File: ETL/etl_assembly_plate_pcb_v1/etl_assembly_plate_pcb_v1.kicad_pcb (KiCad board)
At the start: 2 copper layers, 203.2 x 114.3 mm, 86 parts, among them IC1 PCA9539RPW_Q900J, J1 WP7B-P050VA1-R8000, J2 WP7B-P050VA1-R8000, J3 95278-501A10LF

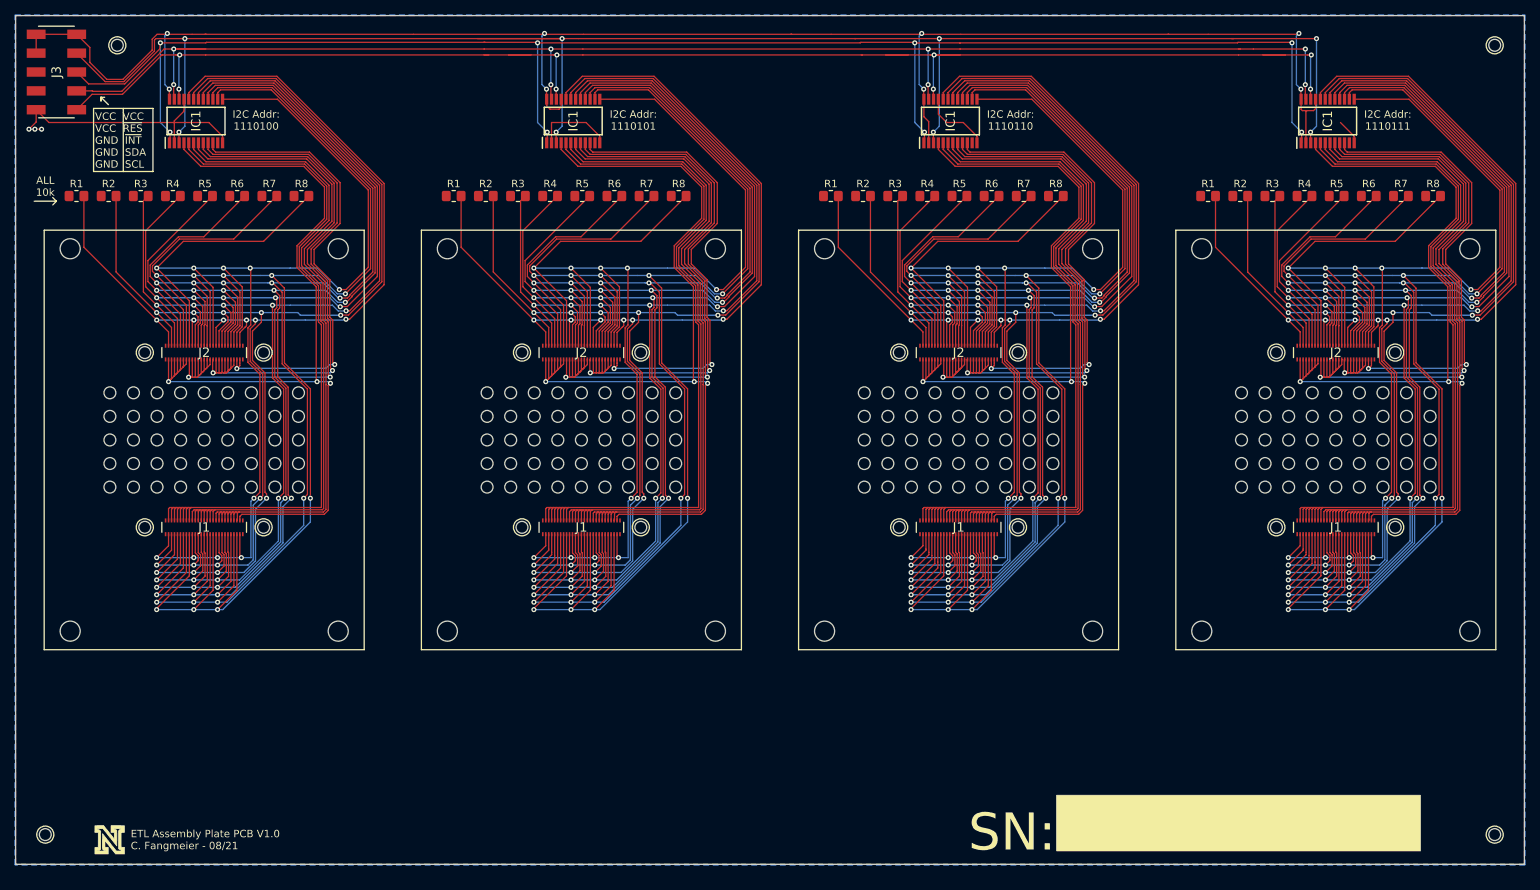
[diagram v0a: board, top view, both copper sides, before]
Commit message: Adds FNAL-mockups and etl_module_pcb_mockup_v2
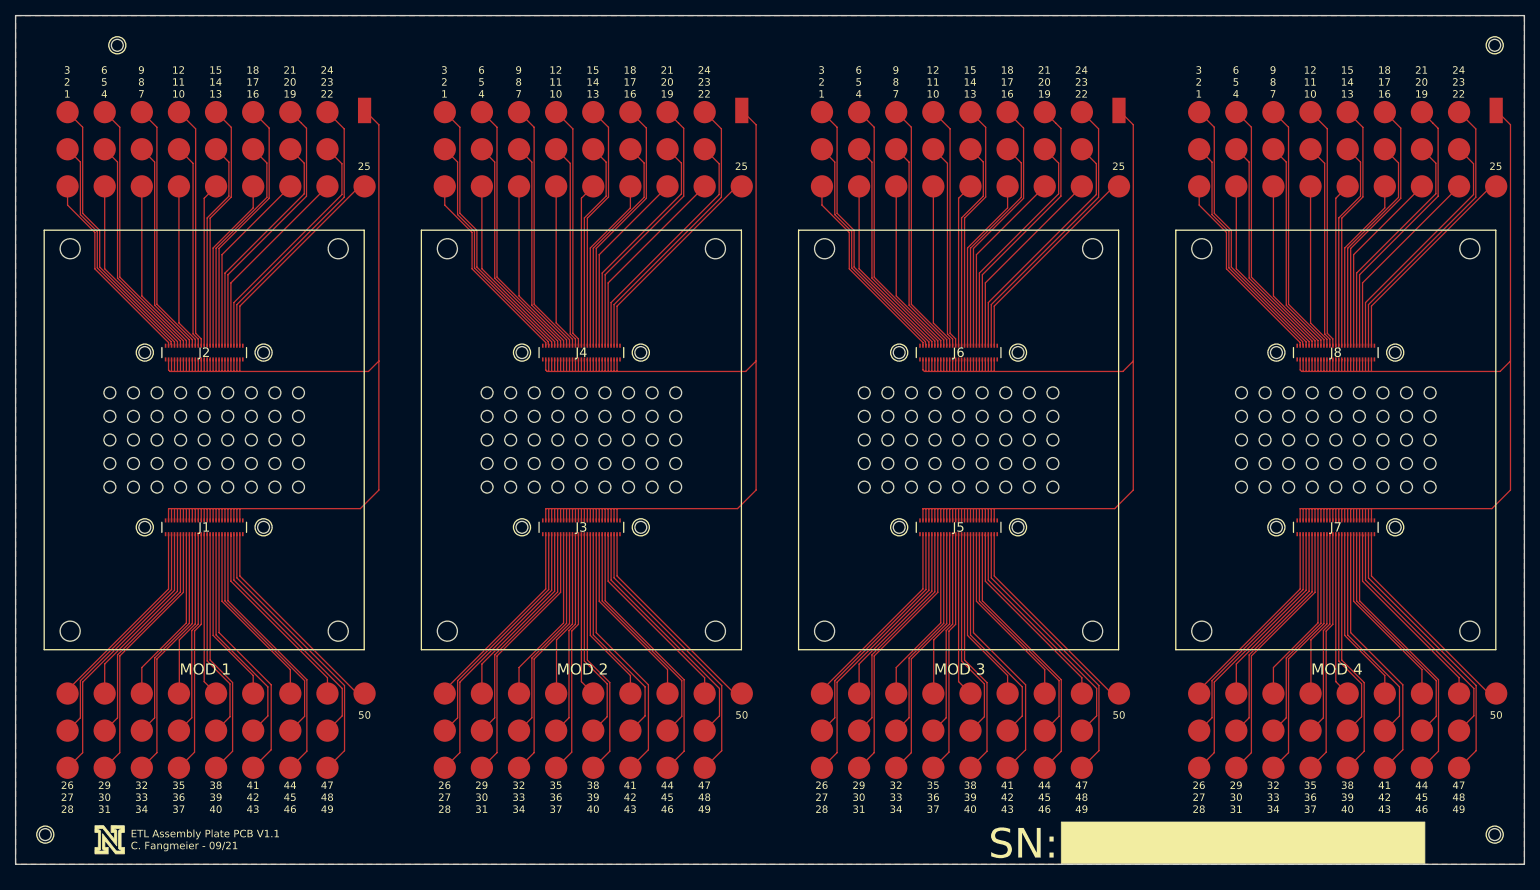
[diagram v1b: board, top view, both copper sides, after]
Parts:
- removed IC1 (x4): PCA9539RPW_Q900J, SamacSys_Parts:SOP65P640X110-24N
- removed the J1 at (177.8, 68.9)
- removed the J1 at (127.0, 68.9)
- removed the J1 at (76.2, 68.9)
- removed the J2 at (177.8, 45.4)
- removed the J2 at (127.0, 45.4)
- removed the J2 at (76.2, 45.4)
- removed R1 (x4), R2 (x4), R3 (x4), R4 (x4), R5 (x4), R6 (x4), R7 (x4), R8 (x4): 10k, Resistor_SMD:R_0805_2012Metric_Pad1.20x1.40mm_HandSolder
- added J4: WP7B-P050VA1-R8000, SamacSys_Parts:WP7BP050VA1R8000, F.Cu at (76.2, 45.4)
- added J5: WP7B-P050VA1-R8000, SamacSys_Parts:WP7BP050VA1R8000, F.Cu at (127.0, 68.9)
- added J6: WP7B-P050VA1-R8000, SamacSys_Parts:WP7BP050VA1R8000, F.Cu at (127.0, 45.4)
- added J7: WP7B-P050VA1-R8000, SamacSys_Parts:WP7BP050VA1R8000, F.Cu at (177.8, 68.9)
- added J8: WP7B-P050VA1-R8000, SamacSys_Parts:WP7BP050VA1R8000, F.Cu at (177.8, 45.4)
- added TP1: TestPoint, unl_silab:TestPoint_Pad_D3.0mm, F.Cu at (159.4, 23.0)
- added TP1: TestPoint, unl_silab:TestPoint_Pad_D3.0mm, F.Cu at (108.6, 23.0)
- added TP1: TestPoint, unl_silab:TestPoint_Pad_D3.0mm, F.Cu at (57.8, 23.0)
- added TP1: TestPoint, unl_silab:TestPoint_Pad_D3.0mm, F.Cu at (7.00, 23.0)
- added TP10: TestPoint, unl_silab:TestPoint_Pad_D3.0mm, F.Cu at (174.4, 23.0)
- added TP10: TestPoint, unl_silab:TestPoint_Pad_D3.0mm, F.Cu at (123.6, 23.0)
- added TP10: TestPoint, unl_silab:TestPoint_Pad_D3.0mm, F.Cu at (72.8, 23.0)
- added TP10: TestPoint, unl_silab:TestPoint_Pad_D3.0mm, F.Cu at (22.0, 23.0)
- added TP11: TestPoint, unl_silab:TestPoint_Pad_D3.0mm, F.Cu at (174.4, 18.0)
- added TP11: TestPoint, unl_silab:TestPoint_Pad_D3.0mm, F.Cu at (123.6, 18.0)
- added TP11: TestPoint, unl_silab:TestPoint_Pad_D3.0mm, F.Cu at (72.8, 18.0)
- added TP11: TestPoint, unl_silab:TestPoint_Pad_D3.0mm, F.Cu at (22.0, 18.0)
- added TP12: TestPoint, unl_silab:TestPoint_Pad_D3.0mm, F.Cu at (174.4, 13.0)
- added TP12: TestPoint, unl_silab:TestPoint_Pad_D3.0mm, F.Cu at (123.6, 13.0)
- added TP12: TestPoint, unl_silab:TestPoint_Pad_D3.0mm, F.Cu at (72.8, 13.0)
- added TP12: TestPoint, unl_silab:TestPoint_Pad_D3.0mm, F.Cu at (22.0, 13.0)
- added TP13: TestPoint, unl_silab:TestPoint_Pad_D3.0mm, F.Cu at (179.4, 23.0)
- added TP13: TestPoint, unl_silab:TestPoint_Pad_D3.0mm, F.Cu at (128.6, 23.0)
- added TP13: TestPoint, unl_silab:TestPoint_Pad_D3.0mm, F.Cu at (77.8, 23.0)
- added TP13: TestPoint, unl_silab:TestPoint_Pad_D3.0mm, F.Cu at (27.0, 23.0)
- added TP14: TestPoint, unl_silab:TestPoint_Pad_D3.0mm, F.Cu at (179.4, 18.0)
- added TP14: TestPoint, unl_silab:TestPoint_Pad_D3.0mm, F.Cu at (128.6, 18.0)
- added TP14: TestPoint, unl_silab:TestPoint_Pad_D3.0mm, F.Cu at (77.8, 18.0)
- added TP14: TestPoint, unl_silab:TestPoint_Pad_D3.0mm, F.Cu at (27.0, 18.0)
- added TP15: TestPoint, unl_silab:TestPoint_Pad_D3.0mm, F.Cu at (179.4, 13.0)
- added TP15: TestPoint, unl_silab:TestPoint_Pad_D3.0mm, F.Cu at (128.6, 13.0)
- added TP15: TestPoint, unl_silab:TestPoint_Pad_D3.0mm, F.Cu at (77.8, 13.0)
- added TP15: TestPoint, unl_silab:TestPoint_Pad_D3.0mm, F.Cu at (27.0, 13.0)
- added TP16: TestPoint, unl_silab:TestPoint_Pad_D3.0mm, F.Cu at (184.4, 23.0)
- added TP16: TestPoint, unl_silab:TestPoint_Pad_D3.0mm, F.Cu at (133.6, 23.0)
- added TP16: TestPoint, unl_silab:TestPoint_Pad_D3.0mm, F.Cu at (82.8, 23.0)
- added TP16: TestPoint, unl_silab:TestPoint_Pad_D3.0mm, F.Cu at (32.0, 23.0)
- added TP17: TestPoint, unl_silab:TestPoint_Pad_D3.0mm, F.Cu at (184.4, 18.0)
- added TP17: TestPoint, unl_silab:TestPoint_Pad_D3.0mm, F.Cu at (133.6, 18.0)
- added TP17: TestPoint, unl_silab:TestPoint_Pad_D3.0mm, F.Cu at (82.8, 18.0)
- added TP17: TestPoint, unl_silab:TestPoint_Pad_D3.0mm, F.Cu at (32.0, 18.0)
- added TP18: TestPoint, unl_silab:TestPoint_Pad_D3.0mm, F.Cu at (184.4, 13.0)
- added TP18: TestPoint, unl_silab:TestPoint_Pad_D3.0mm, F.Cu at (133.6, 13.0)
- added TP18: TestPoint, unl_silab:TestPoint_Pad_D3.0mm, F.Cu at (82.8, 13.0)
- added TP18: TestPoint, unl_silab:TestPoint_Pad_D3.0mm, F.Cu at (32.0, 13.0)
- added TP19: TestPoint, unl_silab:TestPoint_Pad_D3.0mm, F.Cu at (189.4, 23.0)
- added TP19: TestPoint, unl_silab:TestPoint_Pad_D3.0mm, F.Cu at (138.6, 23.0)
- added TP19: TestPoint, unl_silab:TestPoint_Pad_D3.0mm, F.Cu at (87.8, 23.0)
- added TP19: TestPoint, unl_silab:TestPoint_Pad_D3.0mm, F.Cu at (37.0, 23.0)
- added TP2: TestPoint, unl_silab:TestPoint_Pad_D3.0mm, F.Cu at (159.4, 18.0)
- added TP2: TestPoint, unl_silab:TestPoint_Pad_D3.0mm, F.Cu at (108.6, 18.0)
- added TP2: TestPoint, unl_silab:TestPoint_Pad_D3.0mm, F.Cu at (57.8, 18.0)
- added TP2: TestPoint, unl_silab:TestPoint_Pad_D3.0mm, F.Cu at (7.00, 18.0)
- added TP20: TestPoint, unl_silab:TestPoint_Pad_D3.0mm, F.Cu at (189.4, 18.0)
- added TP20: TestPoint, unl_silab:TestPoint_Pad_D3.0mm, F.Cu at (138.6, 18.0)
- added TP20: TestPoint, unl_silab:TestPoint_Pad_D3.0mm, F.Cu at (87.8, 18.0)
- added TP20: TestPoint, unl_silab:TestPoint_Pad_D3.0mm, F.Cu at (37.0, 18.0)
- added TP21: TestPoint, unl_silab:TestPoint_Pad_D3.0mm, F.Cu at (189.4, 13.0)
- added TP21: TestPoint, unl_silab:TestPoint_Pad_D3.0mm, F.Cu at (138.6, 13.0)
- added TP21: TestPoint, unl_silab:TestPoint_Pad_D3.0mm, F.Cu at (87.8, 13.0)
- added TP21: TestPoint, unl_silab:TestPoint_Pad_D3.0mm, F.Cu at (37.0, 13.0)
- added TP22: TestPoint, unl_silab:TestPoint_Pad_D3.0mm, F.Cu at (194.4, 23.0)
- added TP22: TestPoint, unl_silab:TestPoint_Pad_D3.0mm, F.Cu at (143.6, 23.0)
- added TP22: TestPoint, unl_silab:TestPoint_Pad_D3.0mm, F.Cu at (92.8, 23.0)
- added TP22: TestPoint, unl_silab:TestPoint_Pad_D3.0mm, F.Cu at (42.0, 23.0)
- added TP23: TestPoint, unl_silab:TestPoint_Pad_D3.0mm, F.Cu at (194.4, 18.0)
- added TP23: TestPoint, unl_silab:TestPoint_Pad_D3.0mm, F.Cu at (143.6, 18.0)
- added TP23: TestPoint, unl_silab:TestPoint_Pad_D3.0mm, F.Cu at (92.8, 18.0)
- added TP23: TestPoint, unl_silab:TestPoint_Pad_D3.0mm, F.Cu at (42.0, 18.0)
- added TP24: TestPoint, unl_silab:TestPoint_Pad_D3.0mm, F.Cu at (194.4, 13.0)
- added TP24: TestPoint, unl_silab:TestPoint_Pad_D3.0mm, F.Cu at (143.6, 13.0)
- added TP24: TestPoint, unl_silab:TestPoint_Pad_D3.0mm, F.Cu at (92.8, 13.0)
- added TP24: TestPoint, unl_silab:TestPoint_Pad_D3.0mm, F.Cu at (42.0, 13.0)
- added TP25: TestPoint, unl_silab:TestPoint_Pad_D3.0mm, F.Cu at (199.4, 23.0)
- added TP25: TestPoint, unl_silab:TestPoint_Pad_D3.0mm, F.Cu at (148.6, 23.0)
- added TP25: TestPoint, unl_silab:TestPoint_Pad_D3.0mm, F.Cu at (97.8, 23.0)
- added TP25: TestPoint, unl_silab:TestPoint_Pad_D3.0mm, F.Cu at (47.0, 23.0)
- added TP26: TestPoint, unl_silab:TestPoint_Pad_D3.0mm, F.Cu at (159.4, 91.3)
- added TP26: TestPoint, unl_silab:TestPoint_Pad_D3.0mm, F.Cu at (108.6, 91.3)
- added TP26: TestPoint, unl_silab:TestPoint_Pad_D3.0mm, F.Cu at (57.8, 91.3)
- added TP26: TestPoint, unl_silab:TestPoint_Pad_D3.0mm, F.Cu at (7.00, 91.3)
- added TP27: TestPoint, unl_silab:TestPoint_Pad_D3.0mm, F.Cu at (159.4, 96.3)
- added TP27: TestPoint, unl_silab:TestPoint_Pad_D3.0mm, F.Cu at (108.6, 96.3)
- added TP27: TestPoint, unl_silab:TestPoint_Pad_D3.0mm, F.Cu at (57.8, 96.3)
- added TP27: TestPoint, unl_silab:TestPoint_Pad_D3.0mm, F.Cu at (7.00, 96.3)
- added TP28: TestPoint, unl_silab:TestPoint_Pad_D3.0mm, F.Cu at (159.4, 101.3)
- added TP28: TestPoint, unl_silab:TestPoint_Pad_D3.0mm, F.Cu at (108.6, 101.3)
- added TP28: TestPoint, unl_silab:TestPoint_Pad_D3.0mm, F.Cu at (57.8, 101.3)
- added TP28: TestPoint, unl_silab:TestPoint_Pad_D3.0mm, F.Cu at (7.00, 101.3)
- added TP29: TestPoint, unl_silab:TestPoint_Pad_D3.0mm, F.Cu at (164.4, 91.3)
- added TP29: TestPoint, unl_silab:TestPoint_Pad_D3.0mm, F.Cu at (113.6, 91.3)
- added TP29: TestPoint, unl_silab:TestPoint_Pad_D3.0mm, F.Cu at (62.8, 91.3)
- added TP29: TestPoint, unl_silab:TestPoint_Pad_D3.0mm, F.Cu at (12.0, 91.3)
- added TP3: TestPoint, unl_silab:TestPoint_Pad_D3.0mm, F.Cu at (159.4, 13.0)
- added TP3: TestPoint, unl_silab:TestPoint_Pad_D3.0mm, F.Cu at (108.6, 13.0)
- added TP3: TestPoint, unl_silab:TestPoint_Pad_D3.0mm, F.Cu at (57.8, 13.0)
- added TP3: TestPoint, unl_silab:TestPoint_Pad_D3.0mm, F.Cu at (7.00, 13.0)
- added TP30: TestPoint, unl_silab:TestPoint_Pad_D3.0mm, F.Cu at (164.4, 96.3)
- added TP30: TestPoint, unl_silab:TestPoint_Pad_D3.0mm, F.Cu at (113.6, 96.3)
- added TP30: TestPoint, unl_silab:TestPoint_Pad_D3.0mm, F.Cu at (62.8, 96.3)
- added TP30: TestPoint, unl_silab:TestPoint_Pad_D3.0mm, F.Cu at (12.0, 96.3)
- added TP31: TestPoint, unl_silab:TestPoint_Pad_D3.0mm, F.Cu at (164.4, 101.3)
- added TP31: TestPoint, unl_silab:TestPoint_Pad_D3.0mm, F.Cu at (113.6, 101.3)
- added TP31: TestPoint, unl_silab:TestPoint_Pad_D3.0mm, F.Cu at (62.8, 101.3)
- added TP31: TestPoint, unl_silab:TestPoint_Pad_D3.0mm, F.Cu at (12.0, 101.3)
- added TP32: TestPoint, unl_silab:TestPoint_Pad_D3.0mm, F.Cu at (169.4, 91.3)
- added TP32: TestPoint, unl_silab:TestPoint_Pad_D3.0mm, F.Cu at (118.6, 91.3)
- added TP32: TestPoint, unl_silab:TestPoint_Pad_D3.0mm, F.Cu at (67.8, 91.3)
- added TP32: TestPoint, unl_silab:TestPoint_Pad_D3.0mm, F.Cu at (17.0, 91.3)
- added TP33: TestPoint, unl_silab:TestPoint_Pad_D3.0mm, F.Cu at (169.4, 96.3)
- added TP33: TestPoint, unl_silab:TestPoint_Pad_D3.0mm, F.Cu at (118.6, 96.3)
- added TP33: TestPoint, unl_silab:TestPoint_Pad_D3.0mm, F.Cu at (67.8, 96.3)
- added TP33: TestPoint, unl_silab:TestPoint_Pad_D3.0mm, F.Cu at (17.0, 96.3)
- added TP34: TestPoint, unl_silab:TestPoint_Pad_D3.0mm, F.Cu at (169.4, 101.3)
- added TP34: TestPoint, unl_silab:TestPoint_Pad_D3.0mm, F.Cu at (118.6, 101.3)
- added TP34: TestPoint, unl_silab:TestPoint_Pad_D3.0mm, F.Cu at (67.8, 101.3)
- added TP34: TestPoint, unl_silab:TestPoint_Pad_D3.0mm, F.Cu at (17.0, 101.3)
- added TP35: TestPoint, unl_silab:TestPoint_Pad_D3.0mm, F.Cu at (174.4, 91.3)
- added TP35: TestPoint, unl_silab:TestPoint_Pad_D3.0mm, F.Cu at (123.6, 91.3)
- added TP35: TestPoint, unl_silab:TestPoint_Pad_D3.0mm, F.Cu at (72.8, 91.3)
- added TP35: TestPoint, unl_silab:TestPoint_Pad_D3.0mm, F.Cu at (22.0, 91.3)
- added TP36: TestPoint, unl_silab:TestPoint_Pad_D3.0mm, F.Cu at (174.4, 96.3)
- added TP36: TestPoint, unl_silab:TestPoint_Pad_D3.0mm, F.Cu at (123.6, 96.3)
- added TP36: TestPoint, unl_silab:TestPoint_Pad_D3.0mm, F.Cu at (72.8, 96.3)
- added TP36: TestPoint, unl_silab:TestPoint_Pad_D3.0mm, F.Cu at (22.0, 96.3)
- added TP37: TestPoint, unl_silab:TestPoint_Pad_D3.0mm, F.Cu at (174.4, 101.3)
- added TP37: TestPoint, unl_silab:TestPoint_Pad_D3.0mm, F.Cu at (123.6, 101.3)
- added TP37: TestPoint, unl_silab:TestPoint_Pad_D3.0mm, F.Cu at (72.8, 101.3)
- added TP37: TestPoint, unl_silab:TestPoint_Pad_D3.0mm, F.Cu at (22.0, 101.3)
- added TP38: TestPoint, unl_silab:TestPoint_Pad_D3.0mm, F.Cu at (179.4, 91.3)
- added TP38: TestPoint, unl_silab:TestPoint_Pad_D3.0mm, F.Cu at (128.6, 91.3)
- added TP38: TestPoint, unl_silab:TestPoint_Pad_D3.0mm, F.Cu at (77.8, 91.3)
- added TP38: TestPoint, unl_silab:TestPoint_Pad_D3.0mm, F.Cu at (27.0, 91.3)
- added TP39: TestPoint, unl_silab:TestPoint_Pad_D3.0mm, F.Cu at (179.4, 96.3)
- added TP39: TestPoint, unl_silab:TestPoint_Pad_D3.0mm, F.Cu at (128.6, 96.3)
- added TP39: TestPoint, unl_silab:TestPoint_Pad_D3.0mm, F.Cu at (77.8, 96.3)
- added TP39: TestPoint, unl_silab:TestPoint_Pad_D3.0mm, F.Cu at (27.0, 96.3)
- added TP4: TestPoint, unl_silab:TestPoint_Pad_D3.0mm, F.Cu at (164.4, 23.0)
- added TP4: TestPoint, unl_silab:TestPoint_Pad_D3.0mm, F.Cu at (113.6, 23.0)
- added TP4: TestPoint, unl_silab:TestPoint_Pad_D3.0mm, F.Cu at (62.8, 23.0)
- added TP4: TestPoint, unl_silab:TestPoint_Pad_D3.0mm, F.Cu at (12.0, 23.0)
- added TP40: TestPoint, unl_silab:TestPoint_Pad_D3.0mm, F.Cu at (179.4, 101.3)
- added TP40: TestPoint, unl_silab:TestPoint_Pad_D3.0mm, F.Cu at (128.6, 101.3)
- added TP40: TestPoint, unl_silab:TestPoint_Pad_D3.0mm, F.Cu at (77.8, 101.3)
- added TP40: TestPoint, unl_silab:TestPoint_Pad_D3.0mm, F.Cu at (27.0, 101.3)
- added TP41: TestPoint, unl_silab:TestPoint_Pad_D3.0mm, F.Cu at (184.4, 91.3)
- added TP41: TestPoint, unl_silab:TestPoint_Pad_D3.0mm, F.Cu at (133.6, 91.3)
- added TP41: TestPoint, unl_silab:TestPoint_Pad_D3.0mm, F.Cu at (82.8, 91.3)
- added TP41: TestPoint, unl_silab:TestPoint_Pad_D3.0mm, F.Cu at (32.0, 91.3)
- added TP42: TestPoint, unl_silab:TestPoint_Pad_D3.0mm, F.Cu at (184.4, 96.3)
- added TP42: TestPoint, unl_silab:TestPoint_Pad_D3.0mm, F.Cu at (133.6, 96.3)
- added TP42: TestPoint, unl_silab:TestPoint_Pad_D3.0mm, F.Cu at (82.8, 96.3)
- added TP42: TestPoint, unl_silab:TestPoint_Pad_D3.0mm, F.Cu at (32.0, 96.3)
- added TP43: TestPoint, unl_silab:TestPoint_Pad_D3.0mm, F.Cu at (184.4, 101.3)
- added TP43: TestPoint, unl_silab:TestPoint_Pad_D3.0mm, F.Cu at (133.6, 101.3)
- added TP43: TestPoint, unl_silab:TestPoint_Pad_D3.0mm, F.Cu at (82.8, 101.3)
- added TP43: TestPoint, unl_silab:TestPoint_Pad_D3.0mm, F.Cu at (32.0, 101.3)
- added TP44: TestPoint, unl_silab:TestPoint_Pad_D3.0mm, F.Cu at (189.4, 91.3)
- added TP44: TestPoint, unl_silab:TestPoint_Pad_D3.0mm, F.Cu at (138.6, 91.3)
- added TP44: TestPoint, unl_silab:TestPoint_Pad_D3.0mm, F.Cu at (87.8, 91.3)
- added TP44: TestPoint, unl_silab:TestPoint_Pad_D3.0mm, F.Cu at (37.0, 91.3)
- added TP45: TestPoint, unl_silab:TestPoint_Pad_D3.0mm, F.Cu at (189.4, 96.3)
- added TP45: TestPoint, unl_silab:TestPoint_Pad_D3.0mm, F.Cu at (138.6, 96.3)
- added TP45: TestPoint, unl_silab:TestPoint_Pad_D3.0mm, F.Cu at (87.8, 96.3)
- added TP45: TestPoint, unl_silab:TestPoint_Pad_D3.0mm, F.Cu at (37.0, 96.3)
- added TP46: TestPoint, unl_silab:TestPoint_Pad_D3.0mm, F.Cu at (189.4, 101.3)
- added TP46: TestPoint, unl_silab:TestPoint_Pad_D3.0mm, F.Cu at (138.6, 101.3)
- added TP46: TestPoint, unl_silab:TestPoint_Pad_D3.0mm, F.Cu at (87.8, 101.3)
- added TP46: TestPoint, unl_silab:TestPoint_Pad_D3.0mm, F.Cu at (37.0, 101.3)
- added TP47: TestPoint, unl_silab:TestPoint_Pad_D3.0mm, F.Cu at (194.4, 91.3)
- added TP47: TestPoint, unl_silab:TestPoint_Pad_D3.0mm, F.Cu at (143.6, 91.3)
- added TP47: TestPoint, unl_silab:TestPoint_Pad_D3.0mm, F.Cu at (92.8, 91.3)
- added TP47: TestPoint, unl_silab:TestPoint_Pad_D3.0mm, F.Cu at (42.0, 91.3)
- added TP48: TestPoint, unl_silab:TestPoint_Pad_D3.0mm, F.Cu at (194.4, 96.3)
- added TP48: TestPoint, unl_silab:TestPoint_Pad_D3.0mm, F.Cu at (143.6, 96.3)
- added TP48: TestPoint, unl_silab:TestPoint_Pad_D3.0mm, F.Cu at (92.8, 96.3)
- added TP48: TestPoint, unl_silab:TestPoint_Pad_D3.0mm, F.Cu at (42.0, 96.3)
- added TP49: TestPoint, unl_silab:TestPoint_Pad_D3.0mm, F.Cu at (194.4, 101.3)
- added TP49: TestPoint, unl_silab:TestPoint_Pad_D3.0mm, F.Cu at (143.6, 101.3)
- added TP49: TestPoint, unl_silab:TestPoint_Pad_D3.0mm, F.Cu at (92.8, 101.3)
- added TP49: TestPoint, unl_silab:TestPoint_Pad_D3.0mm, F.Cu at (42.0, 101.3)
- added TP5: TestPoint, unl_silab:TestPoint_Pad_D3.0mm, F.Cu at (164.4, 18.0)
- added TP5: TestPoint, unl_silab:TestPoint_Pad_D3.0mm, F.Cu at (113.6, 18.0)
- added TP5: TestPoint, unl_silab:TestPoint_Pad_D3.0mm, F.Cu at (62.8, 18.0)
- added TP5: TestPoint, unl_silab:TestPoint_Pad_D3.0mm, F.Cu at (12.0, 18.0)
- added TP50: TestPoint, unl_silab:TestPoint_Pad_D3.0mm, F.Cu at (199.4, 91.3)
- added TP50: TestPoint, unl_silab:TestPoint_Pad_D3.0mm, F.Cu at (148.6, 91.3)
- added TP50: TestPoint, unl_silab:TestPoint_Pad_D3.0mm, F.Cu at (97.8, 91.3)
- added TP50: TestPoint, unl_silab:TestPoint_Pad_D3.0mm, F.Cu at (47.0, 91.3)
- added TP51: TestPoint, unl_silab:Keystone-5084-Test-Point, F.Cu at (47.0, 12.8)
- added TP52: TestPoint, unl_silab:Keystone-5084-Test-Point, F.Cu at (97.8, 12.8)
- added TP53: TestPoint, unl_silab:Keystone-5084-Test-Point, F.Cu at (148.6, 12.8)
- added TP54: TestPoint, unl_silab:Keystone-5084-Test-Point, F.Cu at (199.4, 12.8)
- added TP6: TestPoint, unl_silab:TestPoint_Pad_D3.0mm, F.Cu at (164.4, 13.0)
- added TP6: TestPoint, unl_silab:TestPoint_Pad_D3.0mm, F.Cu at (113.6, 13.0)
- added TP6: TestPoint, unl_silab:TestPoint_Pad_D3.0mm, F.Cu at (62.8, 13.0)
- added TP6: TestPoint, unl_silab:TestPoint_Pad_D3.0mm, F.Cu at (12.0, 13.0)
- added TP7: TestPoint, unl_silab:TestPoint_Pad_D3.0mm, F.Cu at (169.4, 23.0)
- added TP7: TestPoint, unl_silab:TestPoint_Pad_D3.0mm, F.Cu at (118.6, 23.0)
- added TP7: TestPoint, unl_silab:TestPoint_Pad_D3.0mm, F.Cu at (67.8, 23.0)
- added TP7: TestPoint, unl_silab:TestPoint_Pad_D3.0mm, F.Cu at (17.0, 23.0)
- added TP8: TestPoint, unl_silab:TestPoint_Pad_D3.0mm, F.Cu at (169.4, 18.0)
- added TP8: TestPoint, unl_silab:TestPoint_Pad_D3.0mm, F.Cu at (118.6, 18.0)
- added TP8: TestPoint, unl_silab:TestPoint_Pad_D3.0mm, F.Cu at (67.8, 18.0)
- added TP8: TestPoint, unl_silab:TestPoint_Pad_D3.0mm, F.Cu at (17.0, 18.0)
- added TP9: TestPoint, unl_silab:TestPoint_Pad_D3.0mm, F.Cu at (169.4, 13.0)
- added TP9: TestPoint, unl_silab:TestPoint_Pad_D3.0mm, F.Cu at (118.6, 13.0)
- added TP9: TestPoint, unl_silab:TestPoint_Pad_D3.0mm, F.Cu at (67.8, 13.0)
- added TP9: TestPoint, unl_silab:TestPoint_Pad_D3.0mm, F.Cu at (17.0, 13.0)
- J3: value 95278-501A10LF -> WP7B-P050VA1-R8000; footprint SamacSys_Parts:95278501A10LF -> SamacSys_Parts:WP7BP050VA1R8000
- moved J3 93.6 mm to (76.2, 68.9), turned to 0 degrees
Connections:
- J1 pad 1: /N_A_01 -> /D01
- J1 pad 10: /IN_3 -> /P1
- J1 pad 11: /N_A_06 -> /D06
- J1 pad 12: /IN_3 -> /P1
- J1 pad 13: /N_A_07 -> /D07
- J1 pad 14: /IN_3 -> /P1
- J1 pad 15: /N_A_08 -> /D08
- J1 pad 16: /IN_3 -> /P1
- J1 pad 17: /N_A_01 -> /D09
- J1 pad 18: /IN_2 -> /P1
- J1 pad 19: /N_A_02 -> /D10
- J1 pad 2: /IN_3 -> /P1
- J1 pad 20: /IN_2 -> /P1
- J1 pad 21: /N_A_03 -> /D11
- J1 pad 22: /IN_2 -> /P1
- J1 pad 23: /N_A_04 -> /D12
- J1 pad 24: /IN_2 -> /P1
- J1 pad 25: /N_A_05 -> /D13
- J1 pad 26: /IN_2 -> /P1
- J1 pad 27: /N_A_06 -> /D14
- J1 pad 28: /IN_2 -> /P1
- J1 pad 29: /N_A_07 -> /D15
- J1 pad 3: /N_A_02 -> /D02
- J1 pad 30: /IN_2 -> /P1
- J1 pad 31: /N_A_08 -> /D16
- J1 pad 32: /IN_2 -> /P1
- J1 pad 33: /N_A_01 -> /D17
- J1 pad 34: /IN_1 -> /P1
- J1 pad 35: /N_A_02 -> /D18
- J1 pad 36: /IN_1 -> /P1
- J1 pad 37: /N_A_03 -> /D19
- J1 pad 38: /IN_1 -> /P1
- J1 pad 39: /N_A_04 -> /D20
- J1 pad 4: /IN_3 -> /P1
- J1 pad 40: /IN_1 -> /P1
- J1 pad 41: /N_A_05 -> /D21
- J1 pad 42: /IN_1 -> /P1
- J1 pad 43: /N_A_06 -> /D22
- J1 pad 44: /IN_1 -> /P1
- J1 pad 45: /N_A_07 -> /D23
- J1 pad 46: /IN_1 -> /P1
- J1 pad 47: /N_A_08 -> /D24
- J1 pad 48: /IN_1 -> /P1
- J1 pad 49: /N_A_01 -> /D25
- J1 pad 5: /N_A_03 -> /D03
- J1 pad 50: /IN_4 -> /P1
- J1 pad 6: /IN_3 -> /P1
- J1 pad 7: /N_A_04 -> /D04
- J1 pad 8: /IN_3 -> /P1
- J1 pad 9: /N_A_05 -> /D05
- J2 pad 1: /IN_4 -> /P1
- J2 pad 10: /N_A_06 -> /D30
- J2 pad 11: /IN_4 -> /P1
- J2 pad 12: /N_A_07 -> /D31
- J2 pad 13: /IN_4 -> /P1
- J2 pad 14: /N_A_08 -> /D32
- J2 pad 15: /IN_5 -> /P1
- J2 pad 16: /N_A_01 -> /D33
- J2 pad 17: /IN_5 -> /P1
- J2 pad 18: /N_A_02 -> /D34
- J2 pad 19: /IN_5 -> /P1
- J2 pad 2: /N_A_02 -> /D26
- J2 pad 20: /N_A_03 -> /D35
- J2 pad 21: /IN_5 -> /P1
- J2 pad 22: /N_A_04 -> /D36
- J2 pad 23: /IN_5 -> /P1
- J2 pad 24: /N_A_05 -> /D37
- J2 pad 25: /IN_5 -> /P1
- J2 pad 26: /N_A_06 -> /D38
- J2 pad 27: /IN_5 -> /P1
- J2 pad 28: /N_A_07 -> /D39
- J2 pad 29: /IN_5 -> /P1
- J2 pad 3: /IN_4 -> /P1
- J2 pad 30: /N_A_08 -> /D40
- J2 pad 31: /IN_6 -> /P1
- J2 pad 32: /N_A_01 -> /D41
- J2 pad 33: /IN_6 -> /P1
- J2 pad 34: /N_A_02 -> /D42
- J2 pad 35: /IN_6 -> /P1
- J2 pad 36: /N_A_03 -> /D43
- J2 pad 37: /IN_6 -> /P1
- J2 pad 38: /N_A_04 -> /D44
- J2 pad 39: /IN_6 -> /P1
- J2 pad 4: /N_A_03 -> /D27
- J2 pad 40: /N_A_05 -> /D45
- J2 pad 41: /IN_6 -> /P1
- J2 pad 42: /N_A_06 -> /D46
- J2 pad 43: /IN_6 -> /P1
- J2 pad 44: /N_A_07 -> /D47
- J2 pad 45: /IN_6 -> /P1
- J2 pad 46: /N_A_08 -> /D48
- J2 pad 47: /IN_7 -> /P1
- J2 pad 48: /N_A_01 -> /D49
- J2 pad 49: /IN_7 -> /P1
- J2 pad 5: /IN_4 -> /P1
- J2 pad 50: /N_A_02 -> /D50
- J2 pad 6: /N_A_04 -> /D28
- J2 pad 7: /IN_4 -> /P1
- J2 pad 8: /N_A_05 -> /D29
- J2 pad 9: /IN_4 -> /P1
- J3 pad 1: /VCC -> /D01
- J3 pad 10: /SCL -> /P1
- J3 pad 2: /VCC -> /P1
- J3 pad 3: /VCC -> /D02
- J3 pad 4: /RESETB -> /P1
- J3 pad 5: /GND -> /D03
- J3 pad 6: /INTB -> /P1
- J3 pad 7: /GND -> /D04
- J3 pad 8: /SDA -> /P1
- J3 pad 9: /GND -> /D05
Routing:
- net /N_A_08: track 875.5 -> 0.00 mm, vias 36 -> 0
- net /N_A_07: track 836.7 -> 0.00 mm, vias 36 -> 0
- net /N_A_06: track 792.5 -> 0.00 mm, vias 36 -> 0
- net /N_A_01: track 771.1 -> 0.00 mm, vias 40 -> 0
- net /P1: track 0.00 -> 762.2 mm
- net /N_A_05: track 761.6 -> 0.00 mm, vias 36 -> 0
- net /N_A_04: track 732.7 -> 0.00 mm, vias 36 -> 0
- net /N_A_03: track 713.7 -> 0.00 mm, vias 36 -> 0
- net /N_A_02: track 710.7 -> 0.00 mm, vias 40 -> 0
- net /IN_4: track 477.7 -> 0.00 mm, vias 12 -> 0
- net /IN_3: track 410.9 -> 0.00 mm
- net /IN_2: track 389.5 -> 0.00 mm
- net /IN_1: track 368.4 -> 0.00 mm
- net /IN_5: track 350.0 -> 0.00 mm, vias 8 -> 0
- net /IN_6: track 322.7 -> 0.00 mm, vias 8 -> 0
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- added copper zone on F.Cu, net /P1
- removed copper zone on B.Cu, net /GND
- removed copper zone on F.Cu, net /GND
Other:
- rule pad_to_mask_clearance: 0.0508 -> 0
- board text added: "12 11 10"
- board text added: "15 14 13"
- board text added: "18 17 16"
- board text added: "21 20 19"
- board text added: "24 23 22"
- board text added: "25"
- board text added: "26 27 28"
- board text added: "29 30 31"
- board text added: "3 2 1"
- board text added: "32 33 34"
- board text added: "35 36 37"
- board text added: "38 39 40"
- board text added: "41 42 43"
- board text added: "44 45 46"
- board text added: "47 48 49"
- board text added: "50"
- board text added: "6 5 4"
- board text added: "9 8 7"
- board text added: "ETL Assembly Plate PCB V1.1 C. Fangmeier - 09/21"
- board text added: "MOD 1"
- board text added: "MOD 2"
- board text added: "MOD 3"
- board text added: "MOD 4"
- board text removed: "ALL 10k"
- board text removed: "ETL Assembly Plate PCB V1.0 C. Fangmeier - 08/21"
- board text removed: "I2C Addr: 1110100"
- board text removed: "I2C Addr: 1110101"
- board text removed: "I2C Addr: 1110110"
- board text removed: "I2C Addr: 1110111"
- board text removed: "VCC VCC VCC ~RES~ GND ~INT~ GND SDA GND SCL"
